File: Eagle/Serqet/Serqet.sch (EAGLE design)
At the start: 61 parts

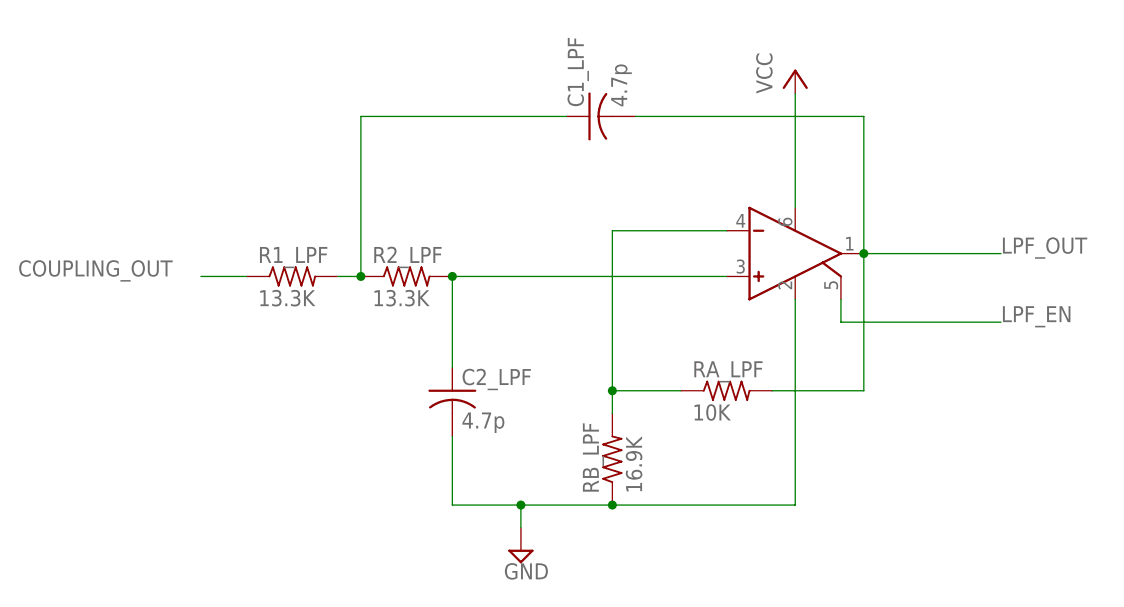
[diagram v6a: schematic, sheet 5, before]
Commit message: Removed LPF Enable
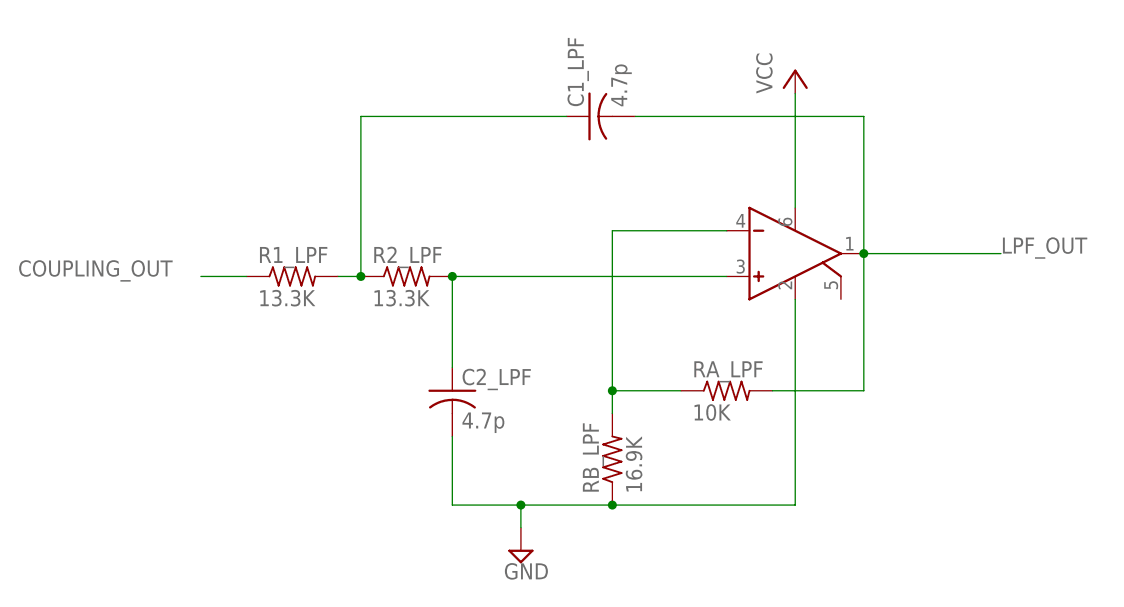
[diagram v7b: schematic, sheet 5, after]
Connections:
- removed net LPF_EN: OP_AMP_LPF.ENABLE
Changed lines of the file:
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@@
-</segment>
-</net>
-<net name="LPF_EN" class="0">
-<segment>
-<pinref part="OP_AMP_LPF" gate="G$1" pin="ENABLE"/>
-<wire x1="45.72" y1="45.72" x2="45.72" y2="43.18" width="0.1524" layer="91"/>
-<wire x1="45.72" y1="43.18" x2="63.5" y2="43.18" width="0.1524" layer="91"/>
-<label x="63.5" y="43.18" size="1.778" layer="95"/>
 </segment>
 </net>
